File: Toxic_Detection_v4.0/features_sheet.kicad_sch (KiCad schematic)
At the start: 16 parts, among them IC1 ESP32-WROOM-32E-N16, J1 Conn_01x11_Pin, SW1 SW_Push

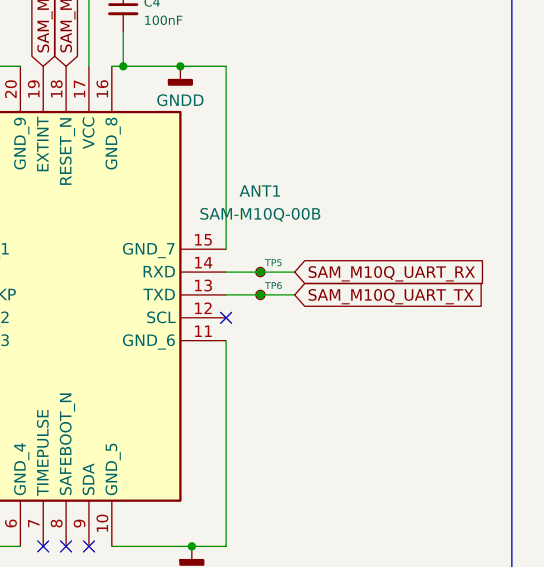
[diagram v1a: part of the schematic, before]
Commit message: feat: take into account all reviews: add anti-aliasing filters, upgrade 3V3 LDO to support up to 5A, fix UART bug between STM and GNSS
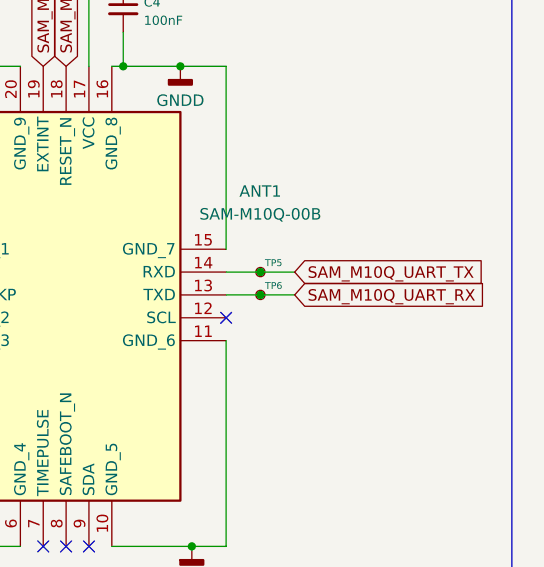
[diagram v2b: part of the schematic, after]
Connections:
- net SAM_M10Q_UART_RX: now also ANT1.13 (TXD), TP6.1; no longer ANT1.14 (RXD), TP5.1
- net SAM_M10Q_UART_TX: now also ANT1.14 (RXD), TP5.1; no longer ANT1.13 (TXD), TP6.1
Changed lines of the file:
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@@
 		(title "Toxic_Detection_PCB")
 		(date "2026-02-12")
-		(rev "4.2")
+		(rev "4.3")
 		(company "Company: LNIS")
 		(comment 4 "Author: Paul Capgras")
@@
 		)
 	)
-	(global_label "SAM_M10Q_UART_RX"
+	(global_label "JTAG_TMS"
+		(shape input)
+		(at 71.12 66.04 180)
+		(fields_autoplaced yes)
+		(effects
+			(font
+				(size 1.27 1.27)
+			)
+			(justify right)
+		)
+		(property "Intersheetrefs" "${INTERSHEET_REFS}"
+			(at 59.2449 66.04 0)
+			(effects
+				(font
+					(size 1.27 1.27)
+				)
+				(justify right)
+				(hide yes)
+			)
+		)
+	)
+	(global_label "ESP32_JTAG_TDO"
+		(shape input)
+		(at 71.12 91.44 180)
+		(fields_autoplaced yes)
+		(effects
+			(font
+				(size 1.27 1.27)
+			)
+			(justify right)
+		)
+		(property "Intersheetrefs" "${INTERSHEET_REFS}"
+			(at 52.2902 91.44 0)
+			(effects
+				(font
+					(size 1.27 1.27)
+				)
+				(justify right)
+				(hide yes)
+			)
+		)
+	)
+	(global_label "STM32_JTAG_TDO__TO__ESP32_JTAG_TDI"
+		(shape input)
+		(at 71.12 68.58 180)
+		(fields_autoplaced yes)
+		(effects
+			(font
+				(size 1.27 1.27)
+			)
+			(justify right)
+		)
+		(property "Intersheetrefs" "${INTERSHEET_REFS}"
+			(at 31.0028 68.58 0)
+			(effects
+				(font
+					(size 1.27 1.27)
+				)
+				(justify right)
+				(hide yes)
+			)
+		)
+	)
+	(global_label "ESP32_SPI_SCLK"
+		(shape input)
+		(at 111.76 48.26 0)
+		(fields_autoplaced yes)
+		(effects
+			(font
+				(size 1.27 1.27)
+			)
+			(justify left)
+		)
+		(property "Intersheetrefs" "${INTERSHEET_REFS}"
+			(at 130.5898 48.26 0)
+			(effects
+				(font
+					(size 1.27 1.27)
+				)
+				(justify left)
+				(hide yes)
+			)
+		)
+	)
+	(global_label "JTAG_TCK"
+		(shape input)
+		(at 71.12 73.66 180)
+		(fields_autoplaced yes)
+		(effects
+			(font
+				(size 1.27 1.27)
+			)
+			(justify right)
+		)
+		(property "Intersheetrefs" "${INTERSHEET_REFS}"
+			(at 59.3658 73.66 0)
+			(effects
+				(font
+					(size 1.27 1.27)
+				)
+				(justify right)
+				(hide yes)
+			)
+		)
+	)
+	(global_label "SAM_M10Q_UART_TX"
 		(shape input)
 		(at 259.08 60.96 0)
@@
 		)
 	)
-	(global_label "JTAG_TMS"
+	(global_label "SAM_M10Q_EXTINT"
 		(shape input)
-		(at 71.12 66.04 180)
-		(fields_autoplaced yes)
-		(effects
-			(font
-				(size 1.27 1.27)
-			)
-			(justify right)
+		(at 231.14 38.1 90)
+		(effects
+			(font
+				(size 1.27 1.27)
+			)
+			(justify left)
 		)
 		(property "Intersheetrefs" "${INTERSHEET_REFS}"
-			(at 59.2449 66.04 0)
-			(effects
-				(font
-					(size 1.27 1.27)
-				)
-				(justify right)
-				(hide yes)
-			)
-		)
-	)
-	(global_label "ESP32_JTAG_TDO"
-		(shape input)
-		(at 71.12 91.44 180)
-		(fields_autoplaced yes)
-		(effects
-			(font
-				(size 1.27 1.27)
-			)
-			(justify right)
-		)
-		(property "Intersheetrefs" "${INTERSHEET_REFS}"
-			(at 52.2902 91.44 0)
-			(effects
-				(font
-					(size 1.27 1.27)
-				)
-				(justify right)
-				(hide yes)
-			)
-		)
-	)
-	(global_label "STM32_JTAG_TDO__TO__ESP32_JTAG_TDI"
-		(shape input)
-		(at 71.12 68.58 180)
-		(fields_autoplaced yes)
-		(effects
-			(font
-				(size 1.27 1.27)
-			)
-			(justify right)
-		)
-		(property "Intersheetrefs" "${INTERSHEET_REFS}"
-			(at 31.0028 68.58 0)
-			(effects
-				(font
-					(size 1.27 1.27)
-				)
-				(justify right)
-				(hide yes)
-			)
-		)
-	)
-	(global_label "ESP32_SPI_SCLK"
-		(shape input)
-		(at 111.76 48.26 0)
-		(fields_autoplaced yes)
-		(effects
-			(font
-				(size 1.27 1.27)
-			)
-			(justify left)
-		)
-		(property "Intersheetrefs" "${INTERSHEET_REFS}"
-			(at 130.5898 48.26 0)
+			(at 231.14 27.94 90)
 			(effects
 				(font
@@
 		)
 	)
-	(global_label "JTAG_TCK"
-		(shape input)
-		(at 71.12 73.66 180)
-		(fields_autoplaced yes)
-		(effects
-			(font
-				(size 1.27 1.27)
-			)
-			(justify right)
-		)
-		(property "Intersheetrefs" "${INTERSHEET_REFS}"
-			(at 59.3658 73.66 0)
-			(effects
-				(font
-					(size 1.27 1.27)
-				)
-				(justify right)
-				(hide yes)
-			)
-		)
-	)
-	(global_label "SAM_M10Q_UART_TX"
+	(global_label "SAM_M10Q_UART_RX"
 		(shape input)
 		(at 259.08 63.5 0)
@@
 			(effects
 				(font
-					(size 1.27 1.27)
-				)
-				(justify left)
-				(hide yes)
-			)
-		)
-	)
-	(global_label "SAM_M10Q_EXTINT"
-		(shape input)
-		(at 231.14 38.1 90)
-		(effects
-			(font
-				(size 1.27 1.27)
-			)
-			(justify left)
-		)
-		(property "Intersheetrefs" "${INTERSHEET_REFS}"
-			(at 231.14 27.94 90)
-			(effects
-				(font
